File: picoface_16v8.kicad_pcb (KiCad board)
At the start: 2 copper layers, 79.2 x 69.6 mm, 23 parts, among them J1 ZX_Spectrum_Connector_48K_SOR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, J2 DE9_Plug, Q1 DMG2305, SW1 SW_USER, SW2 SW_RESET, SW3 SW_RUN, U2 Pico, U3 74LS240

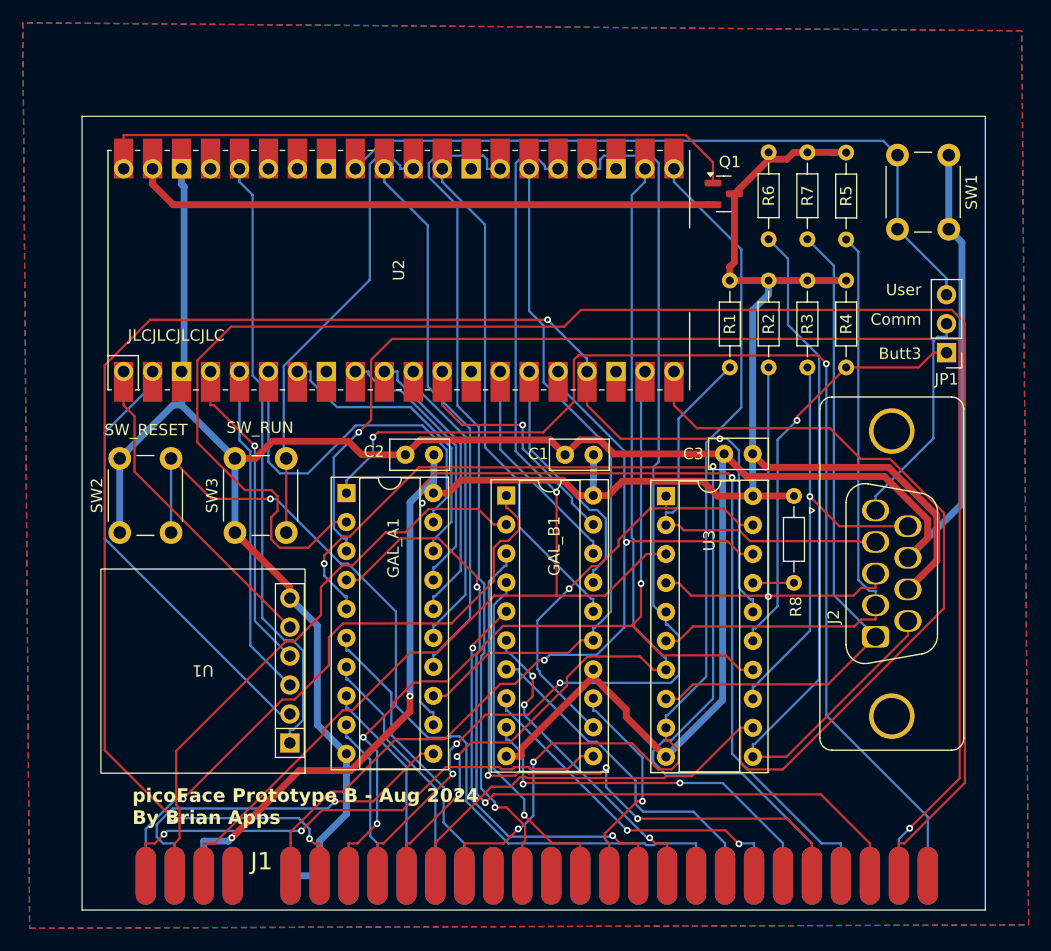
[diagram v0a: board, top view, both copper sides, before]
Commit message: Update to KiCad 9 and add missing gerbers
See issue #1 for details
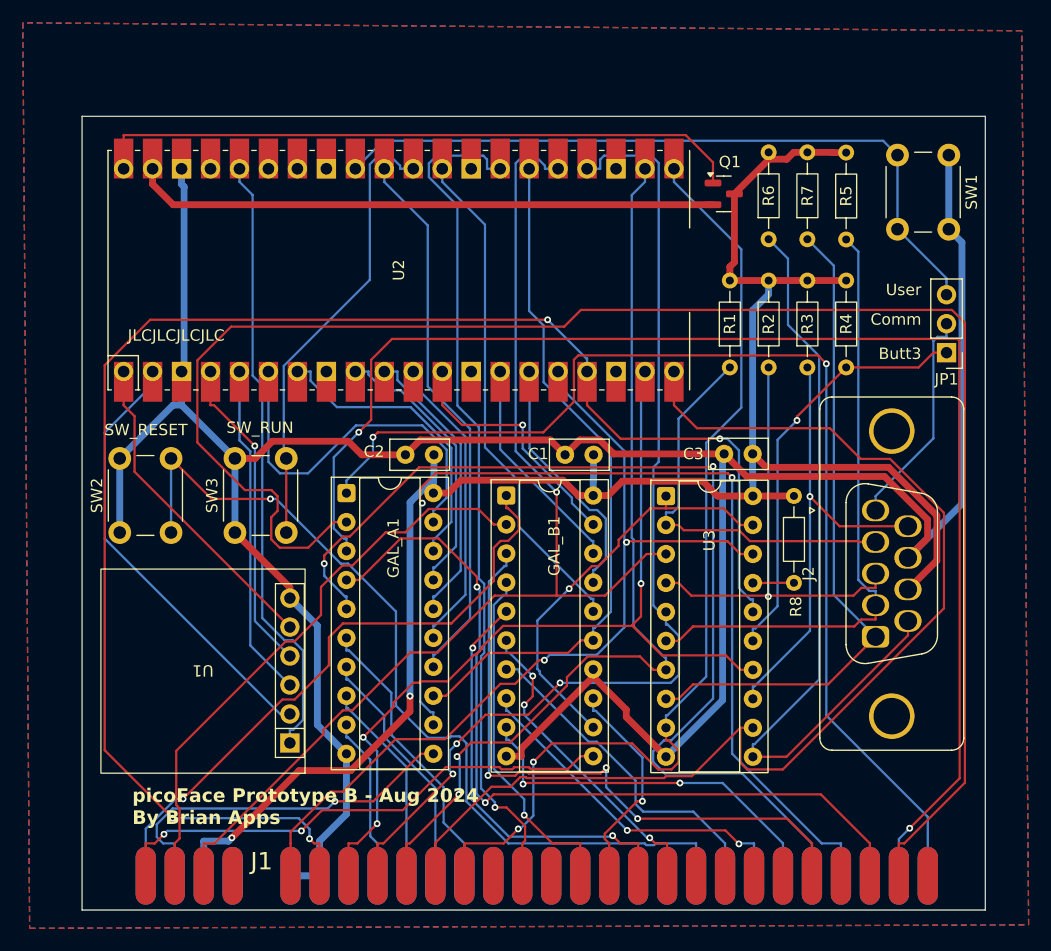
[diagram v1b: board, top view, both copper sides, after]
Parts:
- J1: footprint 8bits:ZX_CONN -> mysyms:ZX_CONN
- J2: footprint 8bits:DSUB-9_Female_Vertical_P2.77x2.84mm_MountingHoles -> mysyms:DSUB-9_Female_Vertical_P2.77x2.84mm_MountingHoles
